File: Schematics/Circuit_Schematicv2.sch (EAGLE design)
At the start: 74 parts, among them Q2 LE33CZ

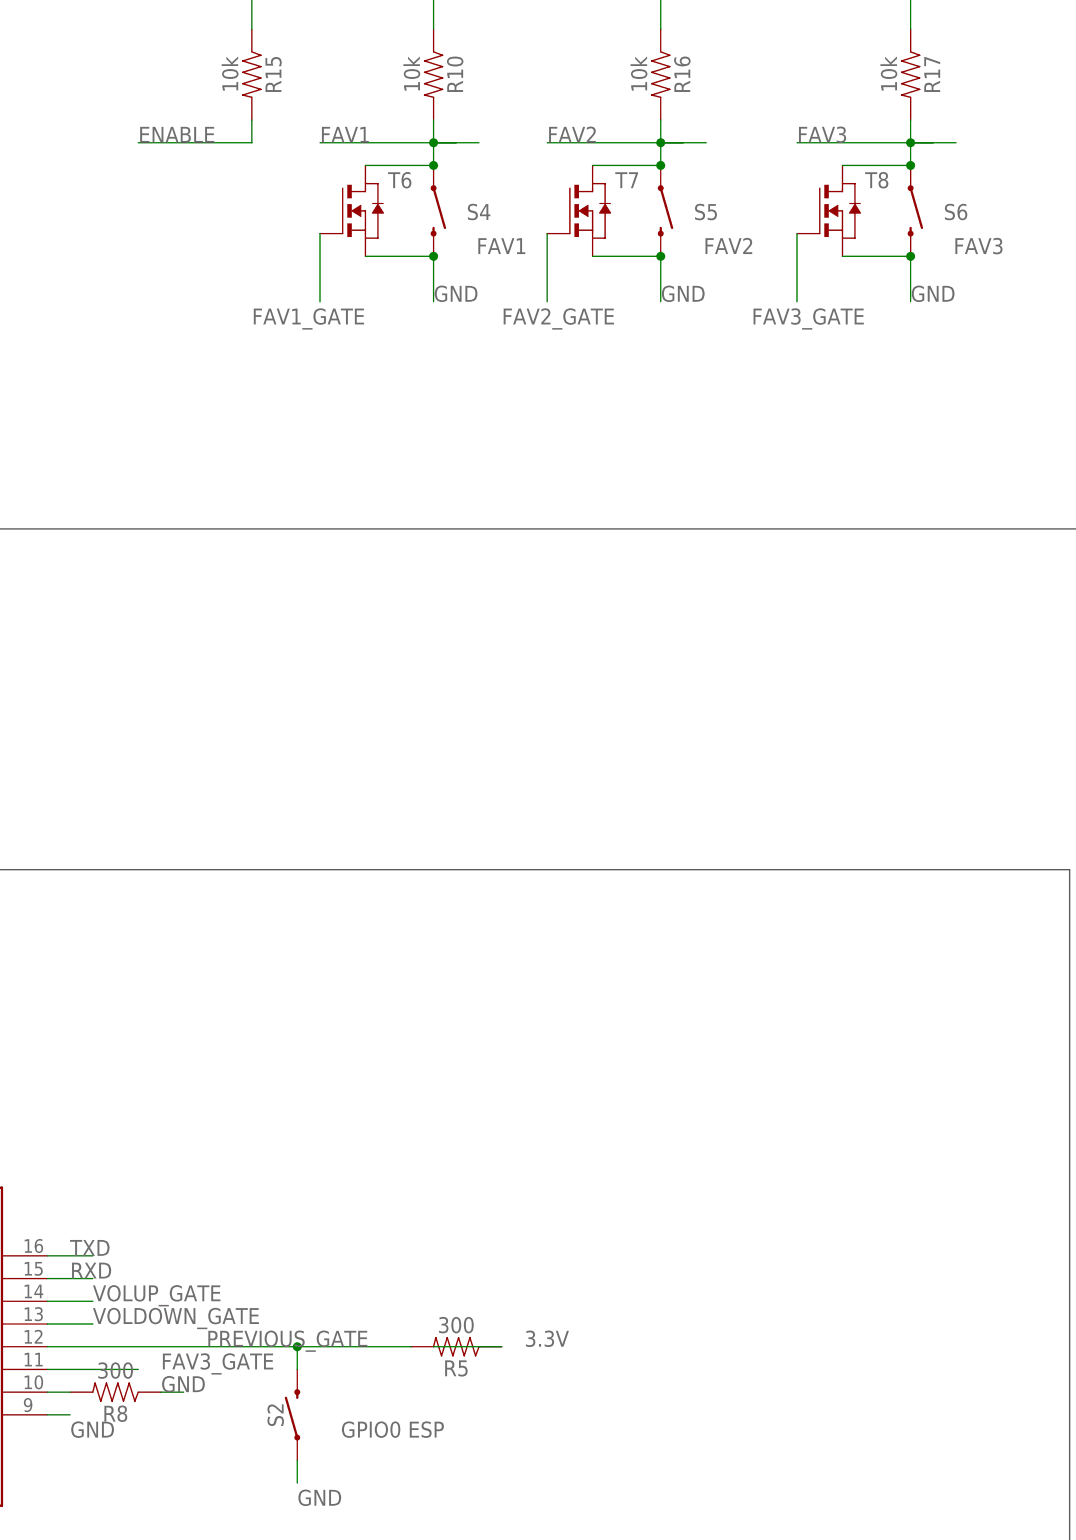
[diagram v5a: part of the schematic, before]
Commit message: Final hardware changes and removed serial monitor from esp code in attempt to reduce noise
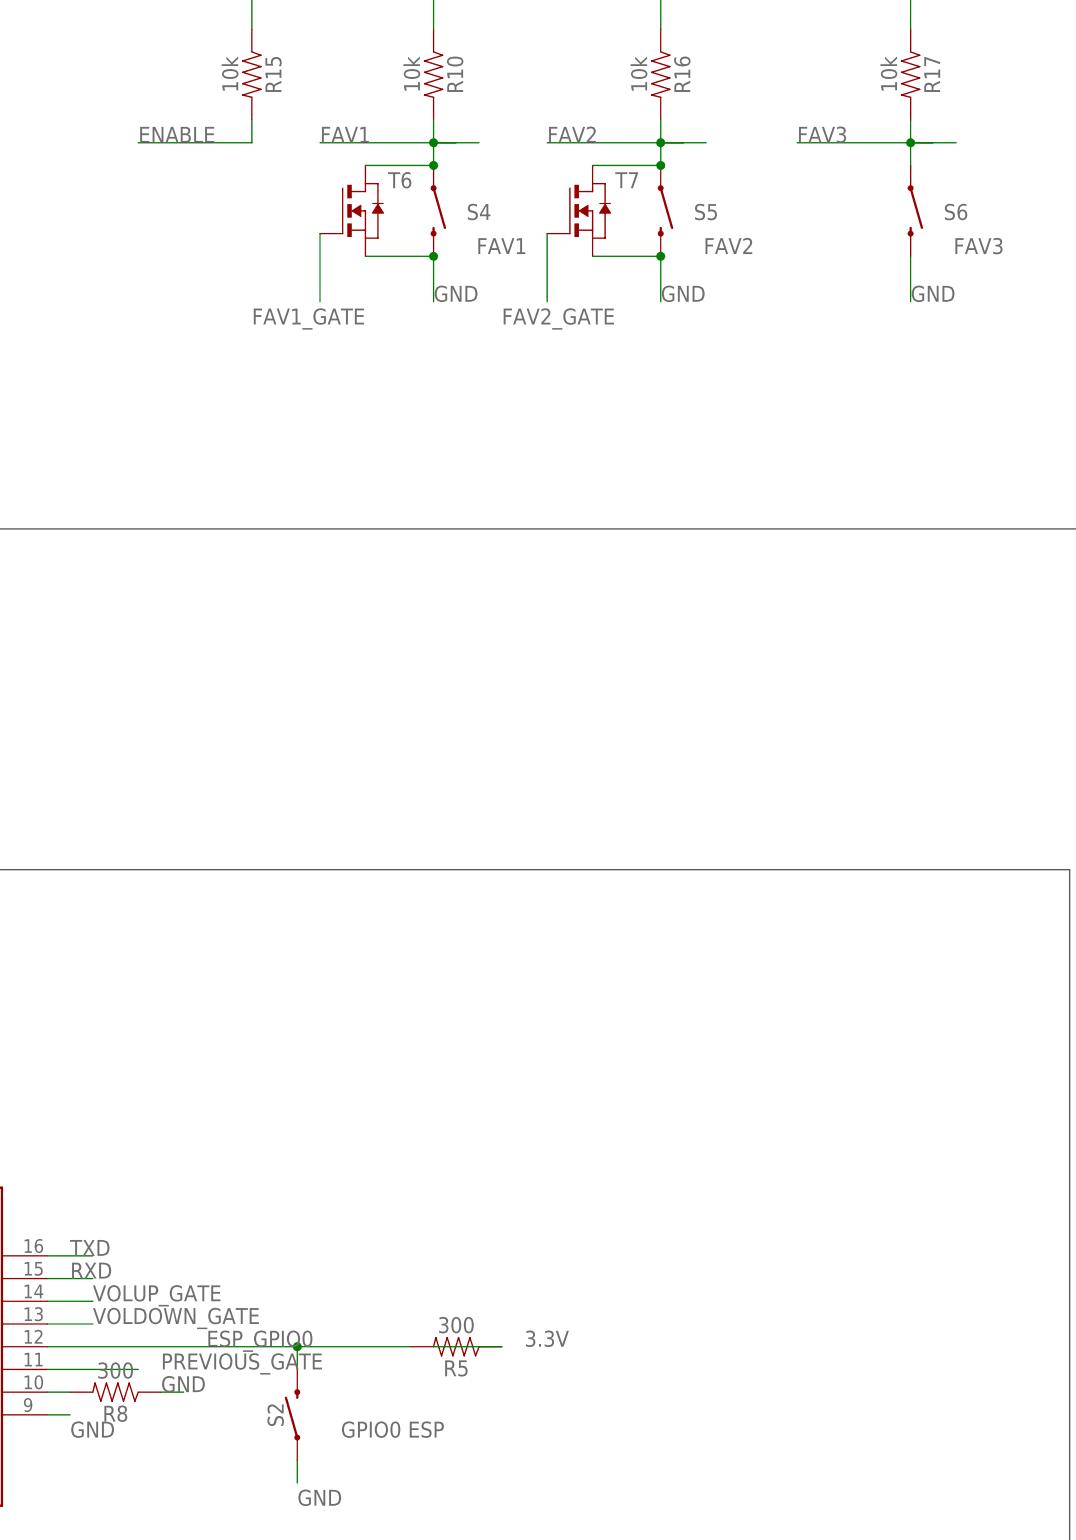
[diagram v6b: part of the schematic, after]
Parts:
- removed T8: (no value), zetex:NMOSSOT223
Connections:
- removed net FAV3_GATE: MDL1.GPIO2, T8.G
- new net ESP_GPIO0: MDL1.GPIO0, R5.2, S2.2
- net FAV3: no longer T8.D
- net GND: no longer T8.S
- net PREVIOUS_GATE: now also MDL1.GPIO2; no longer MDL1.GPIO0, R5.2, S2.2
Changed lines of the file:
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@@
 <part name="T6" library="zetex" deviceset="NMOSSOT223" device=""/>
 <part name="T7" library="zetex" deviceset="NMOSSOT223" device=""/>
-<part name="T8" library="zetex" deviceset="NMOSSOT223" device=""/>
 </parts>
 <sheets>
@@
 <instance part="T6" gate="A" x="439.42" y="180.34"/>
 <instance part="T7" gate="A" x="464.82" y="180.34"/>
-<instance part="T8" gate="A" x="492.76" y="180.34"/>
 </instances>
 <busses>
@@
 <wire x1="500.38" y1="175.26" x2="500.38" y2="170.18" width="0.1524" layer="91"/>
 <label x="500.38" y="170.18" size="1.778" layer="95"/>
-<pinref part="T8" gate="A" pin="S"/>
-<wire x1="492.76" y1="175.26" x2="500.38" y2="175.26" width="0.1524" layer="91"/>
-<junction x="500.38" y="175.26"/>
 </segment>
 <segment>
@@
 <wire x1="502.92" y1="187.96" x2="500.38" y2="187.96" width="0.1524" layer="91"/>
 <wire x1="500.38" y1="187.96" x2="505.46" y2="187.96" width="0.1524" layer="91"/>
-<pinref part="T8" gate="A" pin="D"/>
-<wire x1="492.76" y1="185.42" x2="500.38" y2="185.42" width="0.1524" layer="91"/>
-<junction x="500.38" y="185.42"/>
 </segment>
 <segment>
@@
 </segment>
 <segment>
+<pinref part="MDL1" gate="G$1" pin="GPIO2"/>
+<wire x1="403.86" y1="50.8" x2="414.02" y2="50.8" width="0.1524" layer="91"/>
+<label x="416.56" y="50.8" size="1.778" layer="95"/>
+</segment>
+</net>
+<net name="VOLUP_GATE" class="0">
+<segment>
+<pinref part="T3" gate="A" pin="G"/>
+<wire x1="312.42" y1="177.8" x2="312.42" y2="170.18" width="0.1524" layer="91"/>
+<label x="304.8" y="167.64" size="1.778" layer="95"/>
+</segment>
+<segment>
+<pinref part="MDL1" gate="G$1" pin="GPIO5"/>
+<label x="408.94" y="58.42" size="1.778" layer="95"/>
+<wire x1="403.86" y1="58.42" x2="408.94" y2="58.42" width="0.1524" layer="91"/>
+</segment>
+</net>
+<net name="VOLDOWN_GATE" class="0">
+<segment>
+<pinref part="T4" gate="A" pin="G"/>
+<wire x1="340.36" y1="177.8" x2="340.36" y2="170.18" width="0.1524" layer="91"/>
+<label x="330.2" y="167.64" size="1.778" layer="95"/>
+</segment>
+<segment>
+<pinref part="MDL1" gate="G$1" pin="GPIO4"/>
+<wire x1="408.94" y1="55.88" x2="403.86" y2="55.88" width="0.1524" layer="91"/>
+<label x="408.94" y="55.88" size="1.778" layer="95"/>
+</segment>
+</net>
+<net name="MUTE_GATE" class="0">
+<segment>
+<pinref part="T5" gate="A" pin="G"/>
+<wire x1="375.92" y1="177.8" x2="375.92" y2="170.18" width="0.1524" layer="91"/>
+<label x="368.3" y="167.64" size="1.778" layer="95"/>
+</segment>
+<segment>
+<pinref part="MDL1" gate="G$1" pin="GPIO14"/>
+<wire x1="370.84" y1="53.34" x2="350.52" y2="53.34" width="0.1524" layer="91"/>
+<label x="355.6" y="53.34" size="1.778" layer="95"/>
+</segment>
+</net>
+<net name="FAV1_GATE" class="0">
+<segment>
+<pinref part="T6" gate="A" pin="G"/>
+<wire x1="434.34" y1="177.8" x2="434.34" y2="170.18" width="0.1524" layer="91"/>
+<label x="426.72" y="167.64" size="1.778" layer="95"/>
+</segment>
+<segment>
+<pinref part="MDL1" gate="G$1" pin="GPIO16"/>
+<wire x1="370.84" y1="55.88" x2="363.22" y2="55.88" width="0.1524" layer="91"/>
+<label x="360.68" y="55.88" size="1.778" layer="95"/>
+</segment>
+</net>
+<net name="FAV2_GATE" class="0">
+<segment>
+<pinref part="T7" gate="A" pin="G"/>
+<wire x1="459.74" y1="177.8" x2="459.74" y2="170.18" width="0.1524" layer="91"/>
+<label x="454.66" y="167.64" size="1.778" layer="95"/>
+</segment>
+<segment>
+<pinref part="MDL1" gate="G$1" pin="GPIO13"/>
+<wire x1="370.84" y1="48.26" x2="363.22" y2="48.26" width="0.1524" layer="91"/>
+<label x="360.68" y="48.26" size="1.778" layer="95"/>
+</segment>
+</net>
+<net name="ESP_GPIO0" class="0">
+<segment>
 <pinref part="MDL1" gate="G$1" pin="GPIO0"/>
 <pinref part="R5" gate="G$1" pin="2"/>
@@
 </segment>
 </net>
-<net name="VOLUP_GATE" class="0">
-<segment>
-<pinref part="T3" gate="A" pin="G"/>
-<wire x1="312.42" y1="177.8" x2="312.42" y2="170.18" width="0.1524" layer="91"/>
-<label x="304.8" y="167.64" size="1.778" layer="95"/>
-</segment>
-<segment>
-<pinref part="MDL1" gate="G$1" pin="GPIO5"/>
-<label x="408.94" y="58.42" size="1.778" layer="95"/>
-<wire x1="403.86" y1="58.42" x2="408.94" y2="58.42" width="0.1524" layer="91"/>
-</segment>
-</net>
-<net name="VOLDOWN_GATE" class="0">
-<segment>
-<pinref part="T4" gate="A" pin="G"/>
-<wire x1="340.36" y1="177.8" x2="340.36" y2="170.18" width="0.1524" layer="91"/>
-<label x="330.2" y="167.64" size="1.778" layer="95"/>
-</segment>
-<segment>
-<pinref part="MDL1" gate="G$1" pin="GPIO4"/>
-<wire x1="408.94" y1="55.88" x2="403.86" y2="55.88" width="0.1524" layer="91"/>
-<label x="408.94" y="55.88" size="1.778" layer="95"/>
-</segment>
-</net>
-<net name="MUTE_GATE" class="0">
-<segment>
-<pinref part="T5" gate="A" pin="G"/>
-<wire x1="375.92" y1="177.8" x2="375.92" y2="170.18" width="0.1524" layer="91"/>
-<label x="368.3" y="167.64" size="1.778" layer="95"/>
-</segment>
-<segment>
-<pinref part="MDL1" gate="G$1" pin="GPIO14"/>
-<wire x1="370.84" y1="53.34" x2="350.52" y2="53.34" width="0.1524" layer="91"/>
-<label x="355.6" y="53.34" size="1.778" layer="95"/>
-</segment>
-</net>
-<net name="FAV1_GATE" class="0">
-<segment>
-<pinref part="T6" gate="A" pin="G"/>
-<wire x1="434.34" y1="177.8" x2="434.34" y2="170.18" width="0.1524" layer="91"/>
-<label x="426.72" y="167.64" size="1.778" layer="95"/>
-</segment>
-<segment>
-<pinref part="MDL1" gate="G$1" pin="GPIO16"/>
-<wire x1="370.84" y1="55.88" x2="363.22" y2="55.88" width="0.1524" layer="91"/>
-<label x="360.68" y="55.88" size="1.778" layer="95"/>
-</segment>
-</net>
-<net name="FAV2_GATE" class="0">
-<segment>
-<pinref part="T7" gate="A" pin="G"/>
-<wire x1="459.74" y1="177.8" x2="459.74" y2="170.18" width="0.1524" layer="91"/>
-<label x="454.66" y="167.64" size="1.778" layer="95"/>
-</segment>
-<segment>
-<pinref part="MDL1" gate="G$1" pin="GPIO13"/>
-<wire x1="370.84" y1="48.26" x2="363.22" y2="48.26" width="0.1524" layer="91"/>
-<label x="360.68" y="48.26" size="1.778" layer="95"/>
-</segment>
-</net>
-<net name="FAV3_GATE" class="0">
-<segment>
-<pinref part="T8" gate="A" pin="G"/>
-<wire x1="487.68" y1="177.8" x2="487.68" y2="170.18" width="0.1524" layer="91"/>
-<label x="482.6" y="167.64" size="1.778" layer="95"/>
-</segment>
-<segment>
-<pinref part="MDL1" gate="G$1" pin="GPIO2"/>
-<wire x1="403.86" y1="50.8" x2="414.02" y2="50.8" width="0.1524" layer="91"/>
-<label x="416.56" y="50.8" size="1.778" layer="95"/>
-</segment>
-</net>

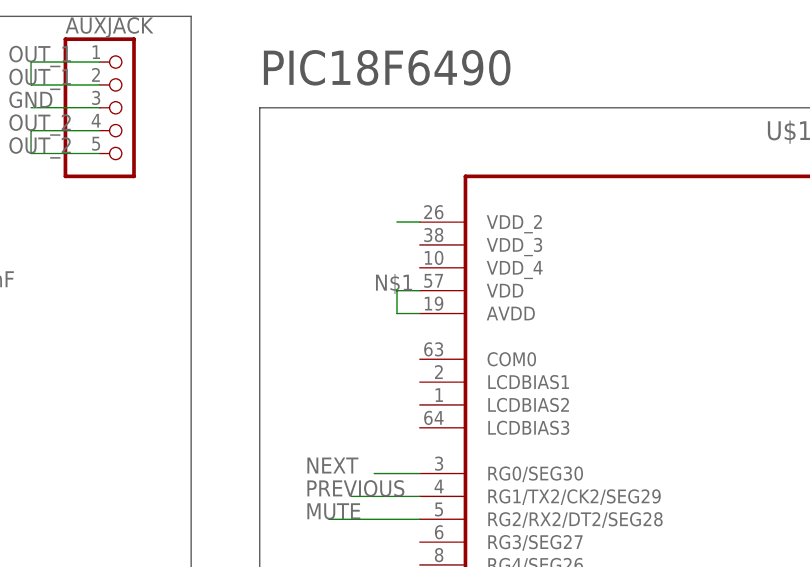
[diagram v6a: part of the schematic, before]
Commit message: Updated the PS for the PIC
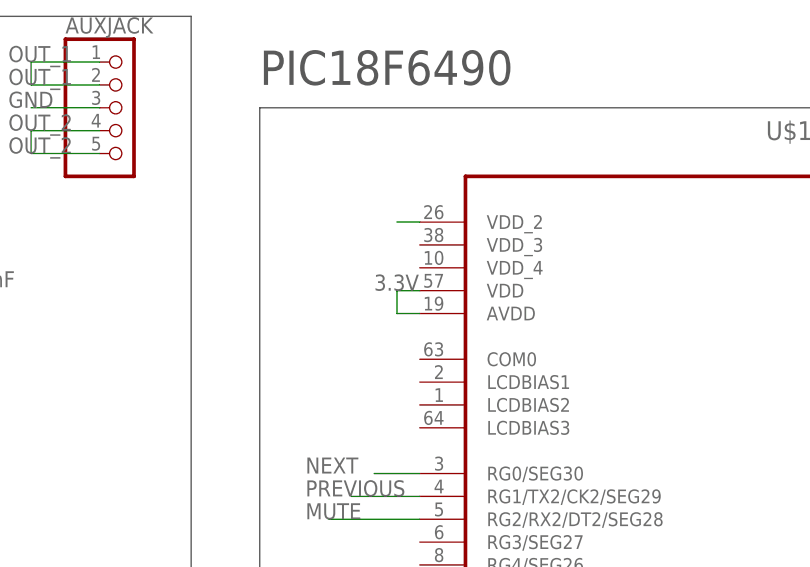
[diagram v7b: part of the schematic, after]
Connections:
- removed net N$1: U$1.AVDD, U$1.VDD
- net 3.3V: now also U$1.AVDD, U$1.VDD
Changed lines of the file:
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@@
 <?xml version="1.0" encoding="utf-8"?>
 <!DOCTYPE eagle SYSTEM "eagle.dtd">
-<eagle version="8.0.0">
+<eagle version="8.1.0">
 <drawing>
 <settings>
@@
 <pinref part="R16" gate="G$1" pin="1"/>
 </segment>
+<segment>
+<pinref part="U$1" gate="A" pin="VDD"/>
+<wire x1="198.12" y1="111.76" x2="195.58" y2="111.76" width="0.1524" layer="91"/>
+<pinref part="U$1" gate="A" pin="AVDD"/>
+<wire x1="198.12" y1="109.22" x2="195.58" y2="109.22" width="0.1524" layer="91"/>
+<wire x1="195.58" y1="109.22" x2="195.58" y2="111.76" width="0.1524" layer="91"/>
+<label x="193.04" y="111.76" size="1.778" layer="95"/>
+</segment>
 </net>
 <net name="L-OUT" class="0">
@@
 </segment>
 </net>
-<net name="N$1" class="0">
-<segment>
-<pinref part="U$1" gate="A" pin="VDD"/>
-<wire x1="198.12" y1="111.76" x2="195.58" y2="111.76" width="0.1524" layer="91"/>
-<pinref part="U$1" gate="A" pin="AVDD"/>
-<wire x1="198.12" y1="109.22" x2="195.58" y2="109.22" width="0.1524" layer="91"/>
-<wire x1="195.58" y1="109.22" x2="195.58" y2="111.76" width="0.1524" layer="91"/>
-<label x="193.04" y="111.76" size="1.778" layer="95"/>
-</segment>
-</net>
